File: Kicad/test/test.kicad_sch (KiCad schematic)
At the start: 74 parts, among them J1 SPKOUT, J2 Tag Con, P1 USB_C_Plug_USB2.0, SW2 SW_Push, SW3 SW_Push, SW4 SW_Push, SW5 SW_Push, U1 MAX98357A, U2 ESP32-S3-WROOM-1, U3 OV5640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

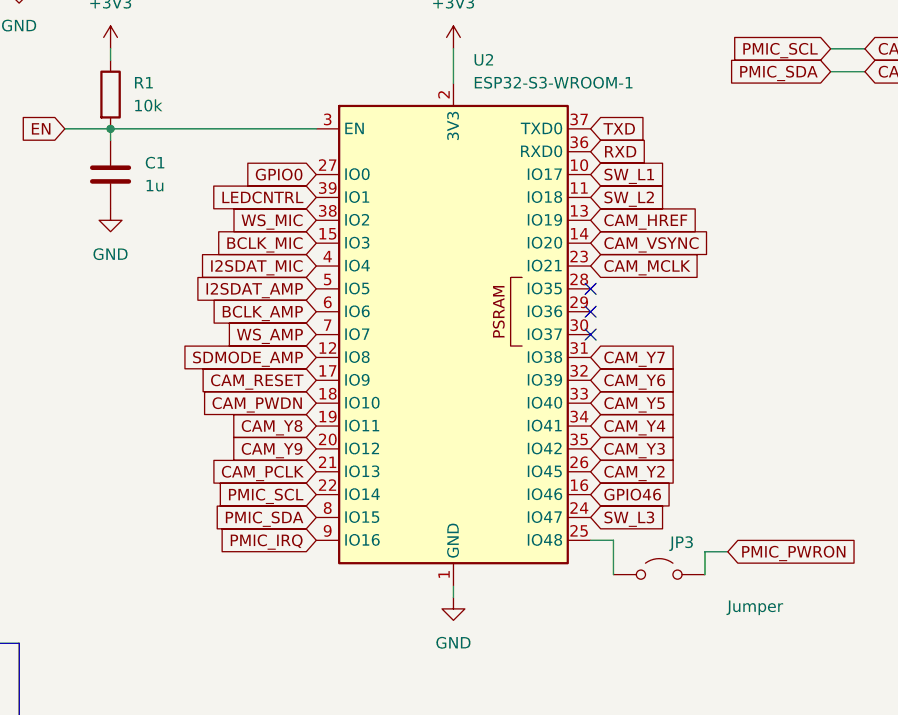
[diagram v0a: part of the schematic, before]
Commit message: Rerouted pin connections on esp32
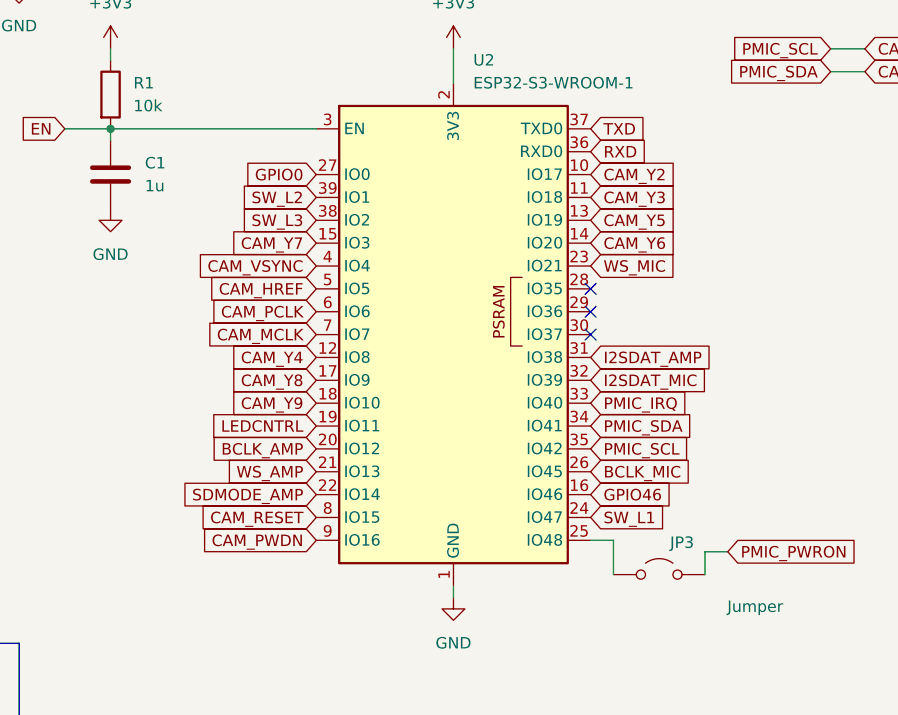
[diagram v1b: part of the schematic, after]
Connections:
- net BCLK_AMP: now also U2.20 (IO12); no longer U2.6 (IO6)
- net BCLK_MIC: now also U2.26 (IO45); no longer U2.15 (IO3)
- net CAM_HREF: now also U2.5 (IO5); no longer U2.13 (IO19)
- net CAM_MCLK: now also U2.7 (IO7); no longer U2.23 (IO21)
- net CAM_PCLK: now also U2.6 (IO6); no longer U2.21 (IO13)
- net CAM_PWDN: now also U2.9 (IO16); no longer U2.18 (IO10)
- net CAM_RESET: now also U2.8 (IO15); no longer U2.17 (IO9)
- net CAM_SCL: now also U2.35 (IO42); no longer U2.22 (IO14)
- net CAM_SDA: now also U2.34 (IO41); no longer U2.8 (IO15)
- net CAM_VSYNC: now also U2.4 (IO4); no longer U2.14 (IO20)
- net CAM_Y2: now also U2.10 (IO17); no longer U2.26 (IO45)
- net CAM_Y3: now also U2.11 (IO18); no longer U2.35 (IO42)
- net CAM_Y4: now also U2.12 (IO8); no longer U2.34 (IO41)
- net CAM_Y5: now also U2.13 (IO19); no longer U2.33 (IO40)
- net CAM_Y6: now also U2.14 (IO20); no longer U2.32 (IO39)
- net CAM_Y7: now also U2.15 (IO3); no longer U2.31 (IO38)
- net CAM_Y8: now also U2.17 (IO9); no longer U2.19 (IO11)
- net CAM_Y9: now also U2.18 (IO10); no longer U2.20 (IO12)
- net I2SDAT_AMP: now also U2.31 (IO38); no longer U2.5 (IO5)
- net I2SDAT_MIC: now also U2.32 (IO39); no longer U2.4 (IO4)
- net LEDCNTRL: now also U2.19 (IO11); no longer U2.39 (IO1)
- net PMIC_IRQ: now also U2.33 (IO40); no longer U2.9 (IO16)
- net SDMODE_AMP: now also U2.22 (IO14); no longer U2.12 (IO8)
- net SW_L1: now also U2.24 (IO47); no longer U2.10 (IO17)
- net SW_L2: now also U2.39 (IO1); no longer U2.11 (IO18)
- net SW_L3: now also U2.38 (IO2); no longer U2.24 (IO47)
- net WS_AMP: now also U2.21 (IO13); no longer U2.7 (IO7)
- net WS_MIC: now also U2.23 (IO21); no longer U2.38 (IO2)

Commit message: Connected a missing piece
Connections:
- net GND: now also JP4.1 (A)
- net at U1.2 (GAIN_SLOT): now also JP4.2 (B)
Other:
- moved on the sheet: JP4
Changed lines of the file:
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@@
 	(wire
 		(pts
+			(xy 220.98 219.71) (xy 220.98 220.98)
+		)
+		(stroke
+			(width 0)
+			(type default)
+		)
+	)
+	(wire
+		(pts
 			(xy 71.12 186.69) (xy 71.12 185.42)
 		)
@@
 	(wire
 		(pts
-			(xy 220.98 217.17) (xy 220.98 218.44)
-		)
-		(stroke
-			(width 0)
-			(type default)
-		)
-	)
-	(wire
-		(pts
 			(xy 111.76 266.7) (xy 111.76 275.59)
 		)
@@
 	(symbol
 		(lib_id "power:GND")
-		(at 220.98 218.44 0)
+		(at 220.98 220.98 0)
 		(unit 1)
 		(exclude_from_sim no)
@@
 		(fields_autoplaced yes)
 		(property "Reference" "#PWR017"
-			(at 220.98 224.79 0)
+			(at 220.98 227.33 0)
 			(effects
 				(font
@@
 		)
 		(property "Value" "GND"
-			(at 220.98 223.52 0)
+			(at 220.98 226.06 0)
 			(effects
 				(font
@@
 		)
 		(property "Footprint" ""
-			(at 220.98 218.44 0)
+			(at 220.98 220.98 0)
 			(effects
 				(font
@@
 		)
 		(property "Datasheet" ""
-			(at 220.98 218.44 0)
+			(at 220.98 220.98 0)
 			(effects
 				(font
@@
 		)
 		(property "Description" "Power symbol creates a global label with name \"GND\" , ground"
-			(at 220.98 218.44 0)
+			(at 220.98 220.98 0)
 			(effects
 				(font
@@
 	(symbol
 		(lib_id "Jumper:Jumper_2_Open")
-		(at 208.28 214.63 0)
+		(at 220.98 214.63 90)
 		(unit 1)
 		(exclude_from_sim yes)
@@
 		(dnp no)
 		(property "Reference" "JP4"
-			(at 210.82 211.074 0)
+			(at 217.424 212.09 0)
 			(effects
 				(font
@@
 		)
 		(property "Value" "Jumper"
-			(at 208.28 217.424 0)
+			(at 223.774 214.63 0)
 			(effects
 				(font
@@
 		)
 		(property "Footprint" "Jumper:SolderJumper-2_P1.3mm_Open_TrianglePad1.0x1.5mm"
-			(at 208.28 214.63 0)
+			(at 220.98 214.63 0)
 			(effects
 				(font
@@
 		)
 		(property "Datasheet" "~"
-			(at 208.28 214.63 0)
+			(at 220.98 214.63 0)
 			(effects
 				(font
@@
 		)
 		(property "Description" "Jumper, 2-pole, open"
-			(at 208.28 214.63 0)
+			(at 220.98 214.63 0)
 			(effects
 				(font

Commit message: 50% Routing Done
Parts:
- removed SW3: SW_Push, switchLibrary:K2-1114SA-A4SW-06, symbol Switch:SW_Push
- added SW1: SW_Push, Library:SW2_1825027-C_TEC, symbol Switch:SW_Push
- SW2: footprint switchLibrary:K2-1114SA-A4SW-06 -> Library:SW2_1825027-C_TEC; LCSC Part C136662 -> C266196; Mfr Part K2-1114SA-A4SW-06 -> 1825027-8
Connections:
- net BCLK_AMP: now also U2.21 (IO13); no longer U2.20 (IO12)
- net GND: now also SW1.1
- net SW_L3: now also SW1.2
- net WS_AMP: now also U2.20 (IO12); no longer U2.21 (IO13)
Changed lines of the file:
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@@
 	(global_label "WS_AMP"
 		(shape input)
-		(at 321.31 214.63 180)
+		(at 321.31 212.09 180)
 		(fields_autoplaced yes)
 		(effects
@@
 		)
 		(property "Intersheetrefs" "${INTERSHEET_REFS}"
-			(at 310.8863 214.63 0)
+			(at 310.8863 212.09 0)
 			(effects
 				(font
@@
 	(global_label "BCLK_AMP"
 		(shape input)
-		(at 321.31 212.09 180)
+		(at 321.31 214.63 180)
 		(fields_autoplaced yes)
 		(effects
@@
 		)
 		(property "Intersheetrefs" "${INTERSHEET_REFS}"
-			(at 308.7091 212.09 0)
+			(at 308.7091 214.63 0)
 			(effects
 				(font
@@
 	)
 	(symbol
+		(lib_id "Switch:SW_Push")
+		(at 241.3 97.79 0)
+		(unit 1)
+		(exclude_from_sim no)
+		(in_bom yes)
+		(on_board yes)
+		(dnp no)
+		(property "Reference" "SW1"
+			(at 241.046 89.662 0)
+			(effects
+				(font
+					(size 1.27 1.27)
+				)
+			)
+		)
+		(property "Value" "SW_Push"
+			(at 241.3 92.71 0)
+			(effects
+				(font
+					(size 1.27 1.27)
+				)
+			)
+		)
+		(property "Footprint" "Library:SW2_1825027-C_TEC"
+			(at 241.3 92.71 0)
+			(effects
+				(font
+					(size 1.27 1.27)
+				)
+				(hide yes)
+			)
+		)
+		(property "Datasheet" "https://www.lcsc.com/datasheet/lcsc_datasheet_2411220707_TE-Connectivity-1825027-8_C266196.pdf"
+			(at 241.3 92.71 0)
+			(effects
+				(font
+					(size 1.27 1.27)
+				)
+				(hide yes)
+			)
+		)
+		(property "Description" "3.25mm Round Button 50mA Bend-in SPST 160gf 24V Plugin Tactile Switches ROHS"
+			(at 241.3 97.79 0)
+			(effects
+				(font
+					(size 1.27 1.27)
+				)
+				(hide yes)
+			)
+		)
+		(property "LCSC Part" "C266196"
+			(at 241.3 97.79 0)
+			(effects
+				(font
+					(size 1.27 1.27)
+				)
+				(hide yes)
+			)
+		)
+		(property "Mfr Part" "1825027-8"
+			(at 241.3 97.79 0)
+			(effects
+				(font
+					(size 1.27 1.27)
+				)
+				(hide yes)
+			)
+		)
+		(pin "1"
+		)
+		(pin "2"
+		)
+		(instances
+			(project "test"
+				(path "/2b9d0de6-8b12-4765-99af-867ac9f145de"
+					(reference "SW1")
+					(unit 1)
+				)
+			)
+		)
+	)
+	(symbol
 		(lib_id "power:GND")
 		(at 288.29 160.02 0)
@@
 	)
 	(symbol
-		(lib_id "Switch:SW_Push")
-		(at 241.3 97.79 0)
-		(unit 1)
-		(exclude_from_sim no)
-		(in_bom yes)
-		(on_board yes)
-		(dnp no)
-		(fields_autoplaced yes)
-		(property "Reference" "SW3"
-			(at 241.3 90.17 0)
-			(effects
-				(font
-					(size 1.27 1.27)
-				)
-			)
-		)
-		(property "Value" "SW_Push"
-			(at 241.3 92.71 0)
-			(effects
-				(font
-					(size 1.27 1.27)
-				)
-			)
-		)
-		(property "Footprint" "switchLibrary:K2-1114SA-A4SW-06"
-			(at 241.3 92.71 0)
-			(effects
-				(font
-					(size 1.27 1.27)
-				)
-				(hide yes)
-			)
-		)
-		(property "Datasheet" "https://www.lcsc.com/datasheet/lcsc_datasheet_1810061013_Korean-Hroparts-Elec-K2-1114SA-A4SW-06_C136662.pdf"
-			(at 241.3 92.71 0)
-			(effects
-				(font
-					(size 1.27 1.27)
-				)
-				(hide yes)
-			)
-		)
-		(property "Description" "3.5mm 1.65mm Rectangle button 50mA Horizontal attachment 4.8mm SPST 100000 Times 250gf 12V SMD Tactile Switches ROHS"
-			(at 241.3 97.79 0)
-			(effects
-				(font
-					(size 1.27 1.27)
-				)
-				(hide yes)
-			)
-		)
-		(property "LCSC Part" "C136662"
-			(at 241.3 97.79 0)
-			(effects
-				(font
-					(size 1.27 1.27)
-				)
-				(hide yes)
-			)
-		)
-		(property "Mfr Part" "K2-1114SA-A4SW-06"
-			(at 241.3 97.79 0)
-			(effects
-				(font
-					(size 1.27 1.27)
-				)
-				(hide yes)
-			)
-		)
-		(pin "1"
-		)
-		(pin "2"
-		)
-		(instances
-			(project "test"
-				(path "/2b9d0de6-8b12-4765-99af-867ac9f145de"
-					(reference "SW3")
-					(unit 1)
-				)
-			)
-		)
-	)
-	(symbol
 		(lib_id "power:+1V5")
 		(at 66.04 186.69 0)
@@
 			)
 		)
-		(property "Footprint" "switchLibrary:K2-1114SA-A4SW-06"
+		(property "Footprint" "Library:SW2_1825027-C_TEC"
 			(at 201.93 91.44 0)
 			(effects
@@
 			)
 		)
-		(property "Datasheet" "https://www.lcsc.com/datasheet/lcsc_datasheet_1810061013_Korean-Hroparts-Elec-K2-1114SA-A4SW-06_C136662.pdf"
+		(property "Datasheet" "https://www.lcsc.com/datasheet/lcsc_datasheet_2411220707_TE-Connectivity-1825027-8_C266196.pdf"
 			(at 201.93 91.44 0)
 			(effects
@@
 			)
 		)
-		(property "Description" "3.5mm 1.65mm Rectangle button 50mA Horizontal attachment 4.8mm SPST 100000 Times 250gf 12V SMD Tactile Switches ROHS"
+		(property "Description" "3.25mm Round Button 50mA Bend-in SPST 160gf 24V Plugin Tactile Switches ROHS"
 			(at 201.93 96.52 0)
 			(effects
@@
 			)
 		)
-		(property "LCSC Part" "C136662"
+		(property "LCSC Part" "C266196"
 			(at 201.93 96.52 0)
 			(effects
@@
 			)
 		)
-		(property "Mfr Part" "K2-1114SA-A4SW-06"
+		(property "Mfr Part" "1825027-8"
 			(at 201.93 96.52 0)
 			(effects

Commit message: ROUTED MORE
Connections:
- net CAM_HREF: now also U2.12 (IO8); no longer U2.5 (IO5)
- net CAM_MCLK: now also U2.18 (IO10); no longer U2.7 (IO7)
- net CAM_PCLK: now also U2.17 (IO9); no longer U2.6 (IO6)
- net CAM_RESET: now also U2.35 (IO42); no longer U2.8 (IO15)
- net CAM_SCL: now also U2.7 (IO7); no longer U2.35 (IO42)
- net CAM_SDA: now also U2.8 (IO15); no longer U2.34 (IO41)
- net CAM_VSYNC: now also U2.34 (IO41); no longer U2.4 (IO4)
- net CAM_Y4: now also U2.4 (IO4); no longer U2.12 (IO8)
- net CAM_Y8: now also U2.5 (IO5); no longer U2.17 (IO9)
- net CAM_Y9: now also U2.6 (IO6); no longer U2.18 (IO10)

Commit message: Routing 80% Done
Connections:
- net SW_L2: now also U2.38 (IO2); no longer U2.39 (IO1)
- net SW_L3: now also U2.39 (IO1); no longer U2.38 (IO2)
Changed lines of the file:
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@@
 	(global_label "SW_L3"
 		(shape input)
+		(at 321.31 184.15 180)
+		(fields_autoplaced yes)
+		(effects
+			(font
+				(size 1.27 1.27)
+			)
+			(justify right)
+		)
+		(property "Intersheetrefs" "${INTERSHEET_REFS}"
+			(at 312.4587 184.15 0)
+			(effects
+				(font
+					(size 1.27 1.27)
+				)
+				(justify right)
+				(hide yes)
+			)
+		)
+	)
+	(global_label "PMIC_PWRON"
+		(shape input)
+		(at 248.92 69.85 0)
+		(fields_autoplaced yes)
+		(effects
+			(font
+				(size 1.27 1.27)
+			)
+			(justify left)
+		)
+		(property "Intersheetrefs" "${INTERSHEET_REFS}"
+			(at 264.1214 69.85 0)
+			(effects
+				(font
+					(size 1.27 1.27)
+				)
+				(justify left)
+				(hide yes)
+			)
+		)
+	)
+	(global_label "CAM_RESET"
+		(shape input)
+		(at 351.79 212.09 0)
+		(fields_autoplaced yes)
+		(effects
+			(font
+				(size 1.27 1.27)
+			)
+			(justify left)
+		)
+		(property "Intersheetrefs" "${INTERSHEET_REFS}"
+			(at 365.2979 212.09 0)
+			(effects
+				(font
+					(size 1.27 1.27)
+				)
+				(justify left)
+				(hide yes)
+			)
+		)
+	)
+	(global_label "CAM_VSYNC"
+		(shape input)
+		(at 351.79 209.55 0)
+		(fields_autoplaced yes)
+		(effects
+			(font
+				(size 1.27 1.27)
+			)
+			(justify left)
+		)
+		(property "Intersheetrefs" "${INTERSHEET_REFS}"
+			(at 365.54 209.55 0)
+			(effects
+				(font
+					(size 1.27 1.27)
+				)
+				(justify left)
+				(hide yes)
+			)
+		)
+	)
+	(global_label "I2SDAT_MIC"
+		(shape input)
+		(at 204.47 264.16 180)
+		(fields_autoplaced yes)
+		(effects
+			(font
+				(size 1.27 1.27)
+			)
+			(justify right)
+		)
+		(property "Intersheetrefs" "${INTERSHEET_REFS}"
+			(at 190.841 264.16 0)
+			(effects
+				(font
+					(size 1.27 1.27)
+				)
+				(justify right)
+				(hide yes)
+			)
+		)
+	)
+	(global_label "CAM_Y9"
+		(shape input)
+		(at 321.31 196.85 180)
+		(fields_autoplaced yes)
+		(effects
+			(font
+				(size 1.27 1.27)
+			)
+			(justify right)
+		)
+		(property "Intersheetrefs" "${INTERSHEET_REFS}"
+			(at 311.2491 196.85 0)
+			(effects
+				(font
+					(size 1.27 1.27)
+				)
+				(justify right)
+				(hide yes)
+			)
+		)
+	)
+	(global_label "CAM_Y4"
+		(shape input)
+		(at 83.82 251.46 180)
+		(fields_autoplaced yes)
+		(effects
+			(font
+				(size 1.27 1.27)
+			)
+			(justify right)
+		)
+		(property "Intersheetrefs" "${INTERSHEET_REFS}"
+			(at 73.7591 251.46 0)
+			(effects
+				(font
+					(size 1.27 1.27)
+				)
+				(justify right)
+				(hide yes)
+			)
+		)
+	)
+	(global_label "CAM_SDA"
+		(shape input)
+		(at 119.38 236.22 0)
+		(fields_autoplaced yes)
+		(effects
+			(font
+				(size 1.27 1.27)
+			)
+			(justify left)
+		)
+		(property "Intersheetrefs" "${INTERSHEET_REFS}"
+			(at 130.7109 236.22 0)
+			(effects
+				(font
+					(size 1.27 1.27)
+				)
+				(justify left)
+				(hide yes)
+			)
+		)
+	)
+	(global_label "CAM_CLKINTRNL"
+		(shape input)
+		(at 128.27 261.62 270)
+		(fields_autoplaced yes)
+		(effects
+			(font
+				(size 1.27 1.27)
+			)
+			(justify right)
+		)
+		(property "Intersheetrefs" "${INTERSHEET_REFS}"
+			(at 128.27 279.4824 90)
+			(effects
+				(font
+					(size 1.27 1.27)
+				)
+				(justify right)
+				(hide yes)
+			)
+		)
+	)
+	(global_label "PMIC_SDA"
+		(shape input)
+		(at 71.12 148.59 180)
+		(fields_autoplaced yes)
+		(effects
+			(font
+				(size 1.27 1.27)
+			)
+			(justify right)
+		)
+		(property "Intersheetrefs" "${INTERSHEET_REFS}"
+			(at 59.0029 148.59 0)
+			(effects
+				(font
+					(size 1.27 1.27)
+				)
+				(justify right)
+				(hide yes)
+			)
+		)
+	)
+	(global_label "LEDCNTRL"
+		(shape input)
+		(at 207.01 149.86 180)
+		(fields_autoplaced yes)
+		(effects
+			(font
+				(size 1.27 1.27)
+			)
+			(justify right)
+		)
+		(property "Intersheetrefs" "${INTERSHEET_REFS}"
+			(at 194.7115 149.86 0)
+			(effects
+				(font
+					(size 1.27 1.27)
+				)
+				(justify right)
+				(hide yes)
+			)
+		)
+	)
+	(global_label "SW_L2"
+		(shape input)
 		(at 321.31 186.69 180)
 		(fields_autoplaced yes)
@@
 			(effects
 				(font
-					(size 1.27 1.27)
-				)
-				(justify right)
-				(hide yes)
-			)
-		)
-	)
-	(global_label "PMIC_PWRON"
-		(shape input)
-		(at 248.92 69.85 0)
-		(fields_autoplaced yes)
-		(effects
-			(font
-				(size 1.27 1.27)
-			)
-			(justify left)
-		)
-		(property "Intersheetrefs" "${INTERSHEET_REFS}"
-			(at 264.1214 69.85 0)
-			(effects
-				(font
-					(size 1.27 1.27)
-				)
-				(justify left)
-				(hide yes)
-			)
-		)
-	)
-	(global_label "CAM_RESET"
-		(shape input)
-		(at 351.79 212.09 0)
-		(fields_autoplaced yes)
-		(effects
-			(font
-				(size 1.27 1.27)
-			)
-			(justify left)
-		)
-		(property "Intersheetrefs" "${INTERSHEET_REFS}"
-			(at 365.2979 212.09 0)
-			(effects
-				(font
-					(size 1.27 1.27)
-				)
-				(justify left)
-				(hide yes)
-			)
-		)
-	)
-	(global_label "CAM_VSYNC"
-		(shape input)
-		(at 351.79 209.55 0)
-		(fields_autoplaced yes)
-		(effects
-			(font
-				(size 1.27 1.27)
-			)
-			(justify left)
-		)
-		(property "Intersheetrefs" "${INTERSHEET_REFS}"
-			(at 365.54 209.55 0)
-			(effects
-				(font
-					(size 1.27 1.27)
-				)
-				(justify left)
-				(hide yes)
-			)
-		)
-	)
-	(global_label "I2SDAT_MIC"
-		(shape input)
-		(at 204.47 264.16 180)
-		(fields_autoplaced yes)
-		(effects
-			(font
-				(size 1.27 1.27)
-			)
-			(justify right)
-		)
-		(property "Intersheetrefs" "${INTERSHEET_REFS}"
-			(at 190.841 264.16 0)
-			(effects
-				(font
-					(size 1.27 1.27)
-				)
-				(justify right)
-				(hide yes)
-			)
-		)
-	)
-	(global_label "CAM_Y9"
-		(shape input)
-		(at 321.31 196.85 180)
-		(fields_autoplaced yes)
-		(effects
-			(font
-				(size 1.27 1.27)
-			)
-			(justify right)
-		)
-		(property "Intersheetrefs" "${INTERSHEET_REFS}"
-			(at 311.2491 196.85 0)
-			(effects
-				(font
-					(size 1.27 1.27)
-				)
-				(justify right)
-				(hide yes)
-			)
-		)
-	)
-	(global_label "CAM_Y4"
-		(shape input)
-		(at 83.82 251.46 180)
-		(fields_autoplaced yes)
-		(effects
-			(font
-				(size 1.27 1.27)
-			)
-			(justify right)
-		)
-		(property "Intersheetrefs" "${INTERSHEET_REFS}"
-			(at 73.7591 251.46 0)
-			(effects
-				(font
-					(size 1.27 1.27)
-				)
-				(justify right)
-				(hide yes)
-			)
-		)
-	)
-	(global_label "CAM_SDA"
-		(shape input)
-		(at 119.38 236.22 0)
-		(fields_autoplaced yes)
-		(effects
-			(font
-				(size 1.27 1.27)
-			)
-			(justify left)
-		)
-		(property "Intersheetrefs" "${INTERSHEET_REFS}"
-			(at 130.7109 236.22 0)
-			(effects
-				(font
-					(size 1.27 1.27)
-				)
-				(justify left)
-				(hide yes)
-			)
-		)
-	)
-	(global_label "CAM_CLKINTRNL"
-		(shape input)
-		(at 128.27 261.62 270)
-		(fields_autoplaced yes)
-		(effects
-			(font
-				(size 1.27 1.27)
-			)
-			(justify right)
-		)
-		(property "Intersheetrefs" "${INTERSHEET_REFS}"
-			(at 128.27 279.4824 90)
-			(effects
-				(font
-					(size 1.27 1.27)
-				)
-				(justify right)
-				(hide yes)
-			)
-		)
-	)
-	(global_label "PMIC_SDA"
-		(shape input)
-		(at 71.12 148.59 180)
-		(fields_autoplaced yes)
-		(effects
-			(font
-				(size 1.27 1.27)
-			)
-			(justify right)
-		)
-		(property "Intersheetrefs" "${INTERSHEET_REFS}"
-			(at 59.0029 148.59 0)
-			(effects
-				(font
-					(size 1.27 1.27)
-				)
-				(justify right)
-				(hide yes)
-			)
-		)
-	)
-	(global_label "LEDCNTRL"
-		(shape input)
-		(at 207.01 149.86 180)
-		(fields_autoplaced yes)
-		(effects
-			(font
-				(size 1.27 1.27)
-			)
-			(justify right)
-		)
-		(property "Intersheetrefs" "${INTERSHEET_REFS}"
-			(at 194.7115 149.86 0)
-			(effects
-				(font
-					(size 1.27 1.27)
-				)
-				(justify right)
-				(hide yes)
-			)
-		)
-	)
-	(global_label "SW_L2"
-		(shape input)
-		(at 321.31 184.15 180)
-		(fields_autoplaced yes)
-		(effects
-			(font
-				(size 1.27 1.27)
-			)
-			(justify right)
-		)
-		(property "Intersheetrefs" "${INTERSHEET_REFS}"
-			(at 312.4587 184.15 0)
-			(effects
-				(font

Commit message: Routing 95% done
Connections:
- net CAM_HREF: now also U2.14 (IO20); no longer U2.12 (IO8)
- net CAM_MCLK: now also U2.12 (IO8); no longer U2.18 (IO10)
- net CAM_PCLK: now also U2.9 (IO16); no longer U2.17 (IO9)
- net CAM_PWDN: now also U2.15 (IO3); no longer U2.9 (IO16)
- net CAM_SCL: now also U2.17 (IO9); no longer U2.7 (IO7)
- net CAM_SDA: now also U2.18 (IO10); no longer U2.8 (IO15)
- net CAM_Y2: now also U2.7 (IO7); no longer U2.10 (IO17)
- net CAM_Y3: now also U2.5 (IO5); no longer U2.11 (IO18)
- net CAM_Y5: now also U2.6 (IO6); no longer U2.13 (IO19)
- net CAM_Y6: now also U2.8 (IO15); no longer U2.14 (IO20)
- net CAM_Y7: now also U2.10 (IO17); no longer U2.15 (IO3)
- net CAM_Y8: now also U2.11 (IO18); no longer U2.5 (IO5)
- net CAM_Y9: now also U2.13 (IO19); no longer U2.6 (IO6)
